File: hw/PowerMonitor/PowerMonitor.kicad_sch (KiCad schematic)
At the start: 21 parts, among them J1 Conn_01x02_Socket, J2 Conn_01x02_Socket, J3 Conn_01x02_Socket, J4 Conn_01x02_Socket, J5 Conn_01x02_Socket, K1 Relay_SPST-NC, U4 NE555D, U5 74LVC1G32, U6 74LVC1G32

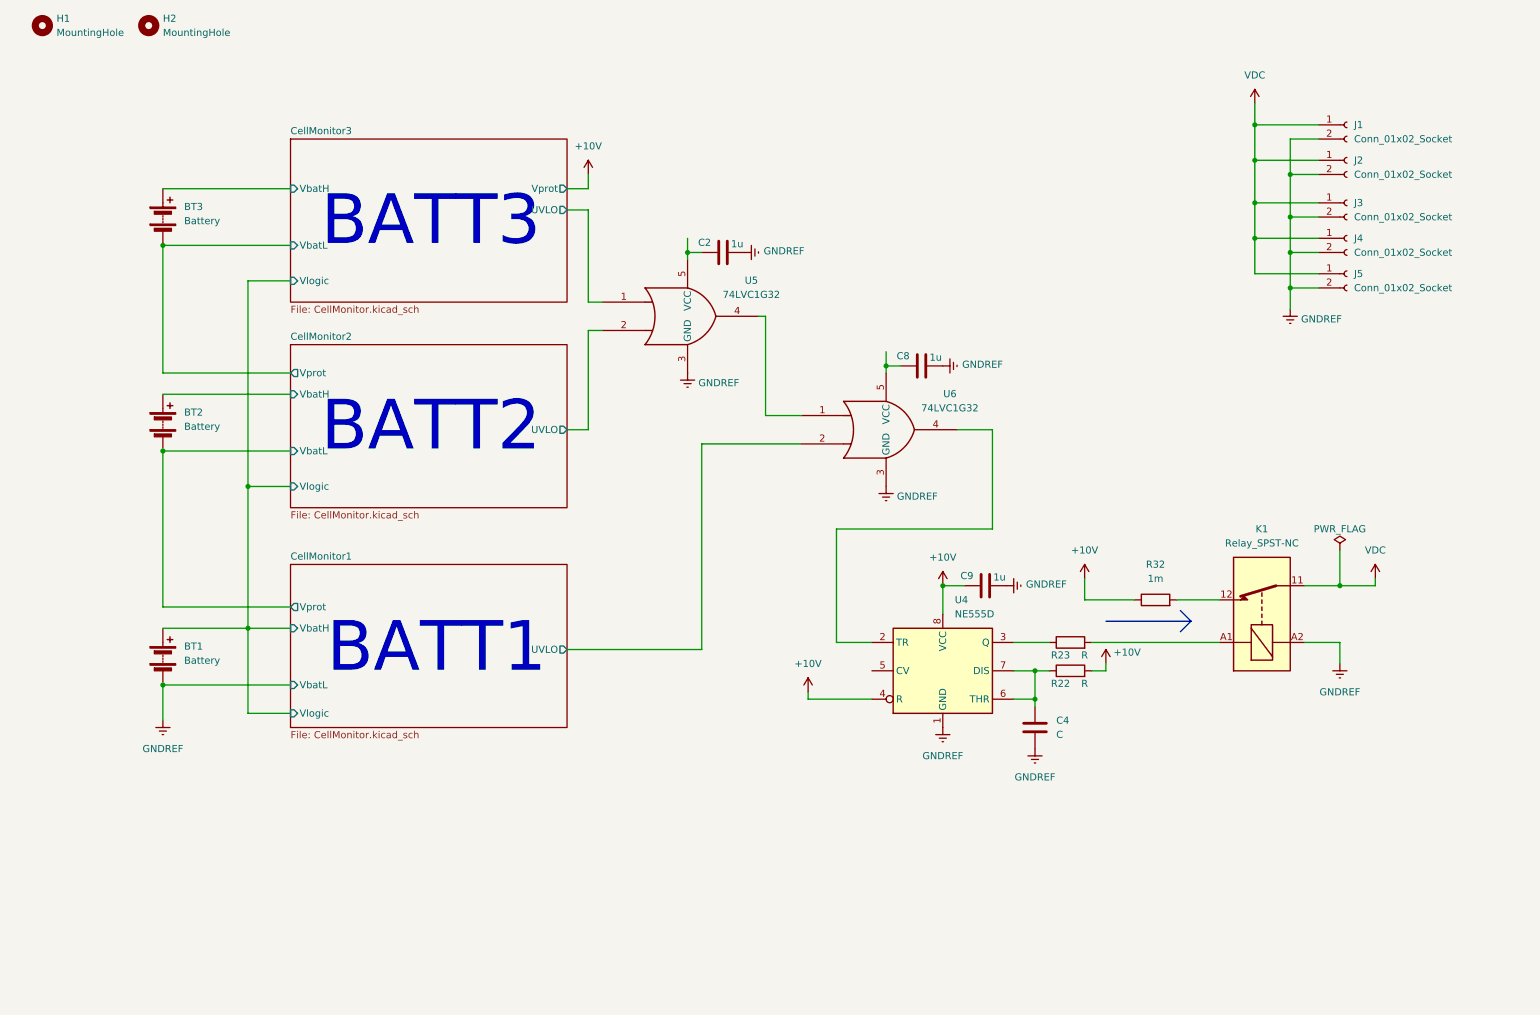
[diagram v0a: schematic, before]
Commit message: preliminar design for battery power monitor, add sd card to fmu
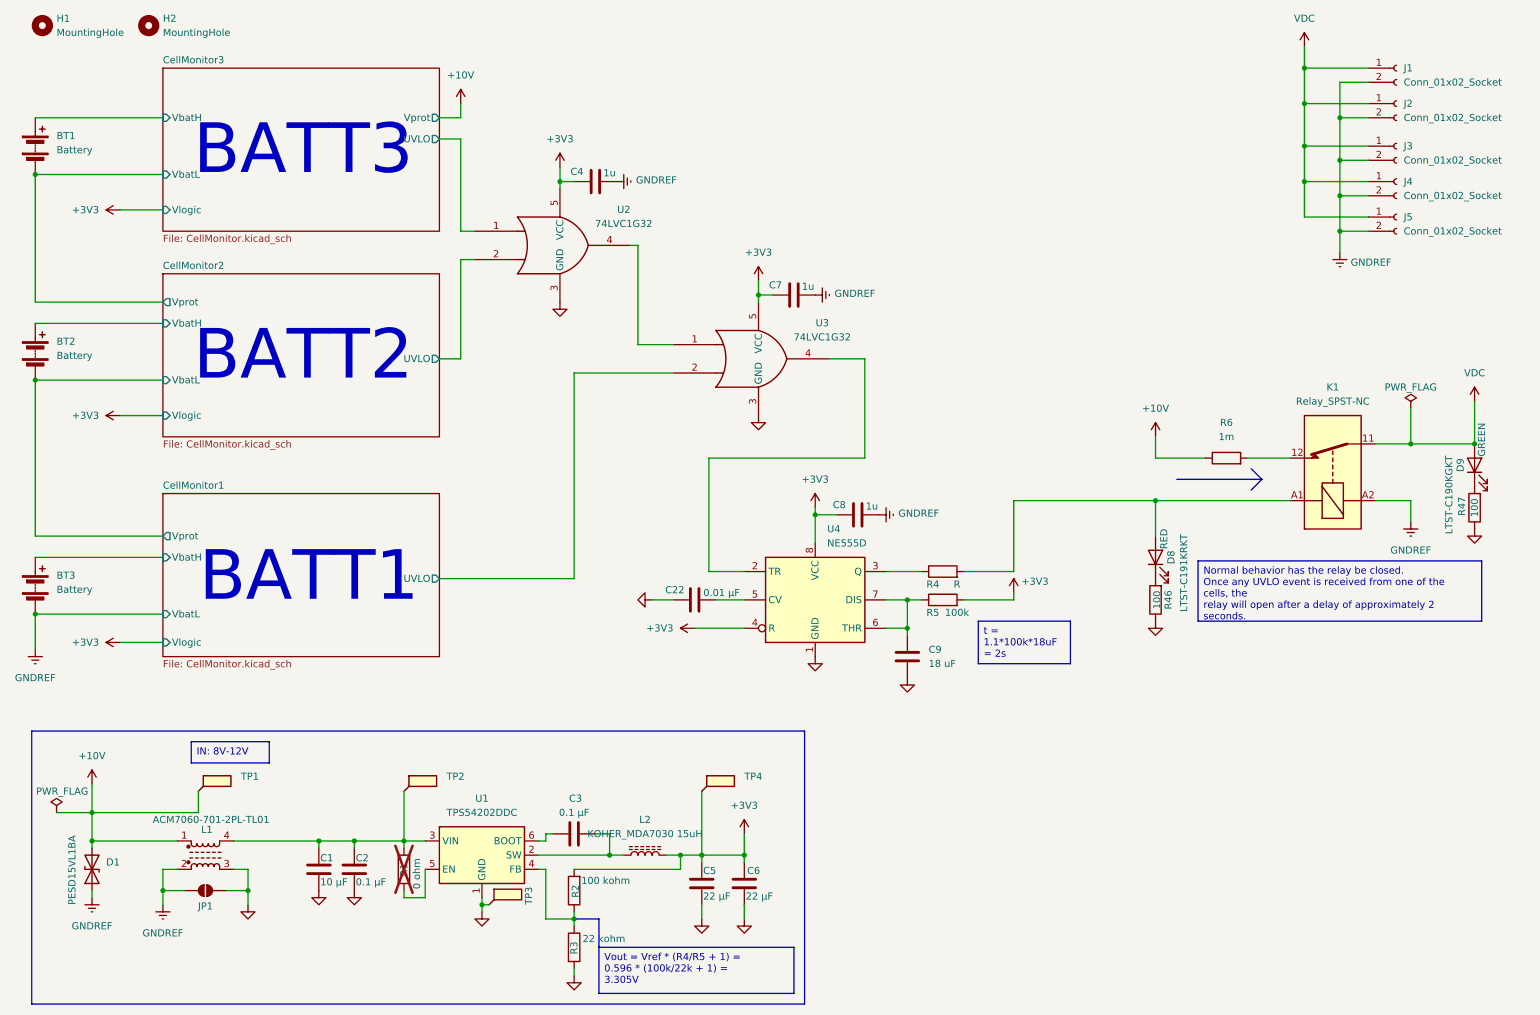
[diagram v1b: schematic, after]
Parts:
- added C1: 10 µF, Capacitor_SMD:C_0603_1608Metric_Pad1.08x0.95mm_HandSolder, symbol #inventree:CL21A106KOQNNNE
- added C2, C3: 0.1 µF, Capacitor_SMD:C_0603_1608Metric_Pad1.08x0.95mm_HandSolder, symbol #inventree:CL21B104KBCNNNC
- added C22: 0.01 µF, Capacitor_SMD:C_0603_1608Metric_Pad1.08x0.95mm_HandSolder, symbol #inventree:CL21B104KBCNNNC
- added C5, C6: 22 µF, Capacitor_SMD:C_0603_1608Metric_Pad1.08x0.95mm_HandSolder, symbol #inventree:CL21X226MOYNNWE
- added D1: PESD15VL1BA, Diode_SMD:D_SOD-323_HandSoldering, symbol Device:D_TVS
- added D8: RED, LED_SMD:LED_0603_1608Metric, symbol Device:LED
- added D9: GREEN, LED_SMD:LED_0603_1608Metric, symbol Device:LED
- added JP1: SolderJumper_2_Open, Jumper:SolderJumper-2_P1.3mm_Open_RoundedPad1.0x1.5mm, symbol Jumper:SolderJumper_2_Open
- added L1: L_Ferrite_Coupled_1423, Inductor_SMD:L_CommonModeChoke_TDK_ACM7060, symbol Device:L_Ferrite_Coupled_1423
- added L2: KOHER_MDA7030 15uH, Inductor_SMD:L_KOHERelec_MDA7030, symbol Device:L_Ferrite
- added R1: 0 ohm, Resistor_SMD:R_0603_1608Metric_Pad0.98x0.95mm_HandSolder, symbol #inventree:RC0603FR-070RL
- added R2: 100 kohm, Resistor_SMD:R_0603_1608Metric_Pad0.98x0.95mm_HandSolder, symbol #inventree:RC0603FR-07100KL
- added R3: 22 kohm, Resistor_SMD:R_0603_1608Metric_Pad0.98x0.95mm_HandSolder, symbol #inventree:RC0603FR-0722KL
- added R46, R47: 100, Resistor_SMD:R_0603_1608Metric, symbol Device:R
- added TP1, TP2, TP3, TP4: TestPoint_Flag, TestPoint:TestPoint_Pad_1.0x1.0mm, symbol Connector:TestPoint_Flag
- added U1: TPS54202DDC, Package_TO_SOT_SMD:SOT-23-6_Handsoldering, symbol Regulator_Switching:TPS54202DDC
- C9: renamed from C4; value C -> 18 uF
- R5: renamed from R22; value R -> 100k
- renumbered BT3 to BT1, BT1 to BT3, C2 to C4, C8 to C7, C9 to C8, R23 to R4, R32 to R6, U5 to U2, U6 to U3
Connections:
- net +10V: now also D1.2 (A2), L1.1, TP1.1; no longer C8.1, R5.2, U4.4 (R), U4.8 (VCC)
- net GNDREF: now also D1.1 (A1), JP1.1 (A), L1.2; no longer C9.2, U2.3 (GND), U3.3 (GND), U4.1 (GND)
- net VDC: now also D9.2 (A)
- net at U4.5 (CV): now also C22.2
- net at K1.A1, R4.2: now also D8.2 (A)
- net +3V3: now reaches C7.1, U3.5 (VCC)
- net +3V3: now also C4.1, C8.1, R5.2, U2.5 (VCC), U4.4 (R), U4.8 (VCC), C5.1, C6.1, L2.2, R2.2, TP4.1
- new net: C3.1, U1.6 (BOOT)
- new net: C3.2, L2.1, U1.2 (SW)
- new net: C1.1, C2.1, L1.4, R1.1, TP2.1, U1.3 (VIN)
- new net: R1.2, U1.5 (EN)
- new net: D9.1 (K), R47.2
- new net: D8.1 (K), R46.2
- new net: R2.1, R3.1, U1.4 (FB)
- new net GND: C1.2, C2.2, C22.1, C5.2, C6.2, C9.2, JP1.2 (B), L1.3, R3.2, R46.1, R47.1, TP3.1, U1.1 (GND), U2.3 (GND), U3.3 (GND), U4.1 (GND)
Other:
- moved on the sheet: BT1, BT2, BT3, C4, C7, C8, C9, J1, J2, J3, J4, J5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
